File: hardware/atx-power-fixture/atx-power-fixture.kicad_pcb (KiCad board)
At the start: 4 copper layers, 111.8 x 64.4 mm, 33 parts, among them J1 ATX24RH, J2 Screw_Terminal_01x02, J3 BINDING_POST, J4 BINDING_POST, J5 Console FTDI, Q1 DMG2301L, Q2 2N7002, SW1 SW_SPST, SW2 SW_SPST, U1 SSD1306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

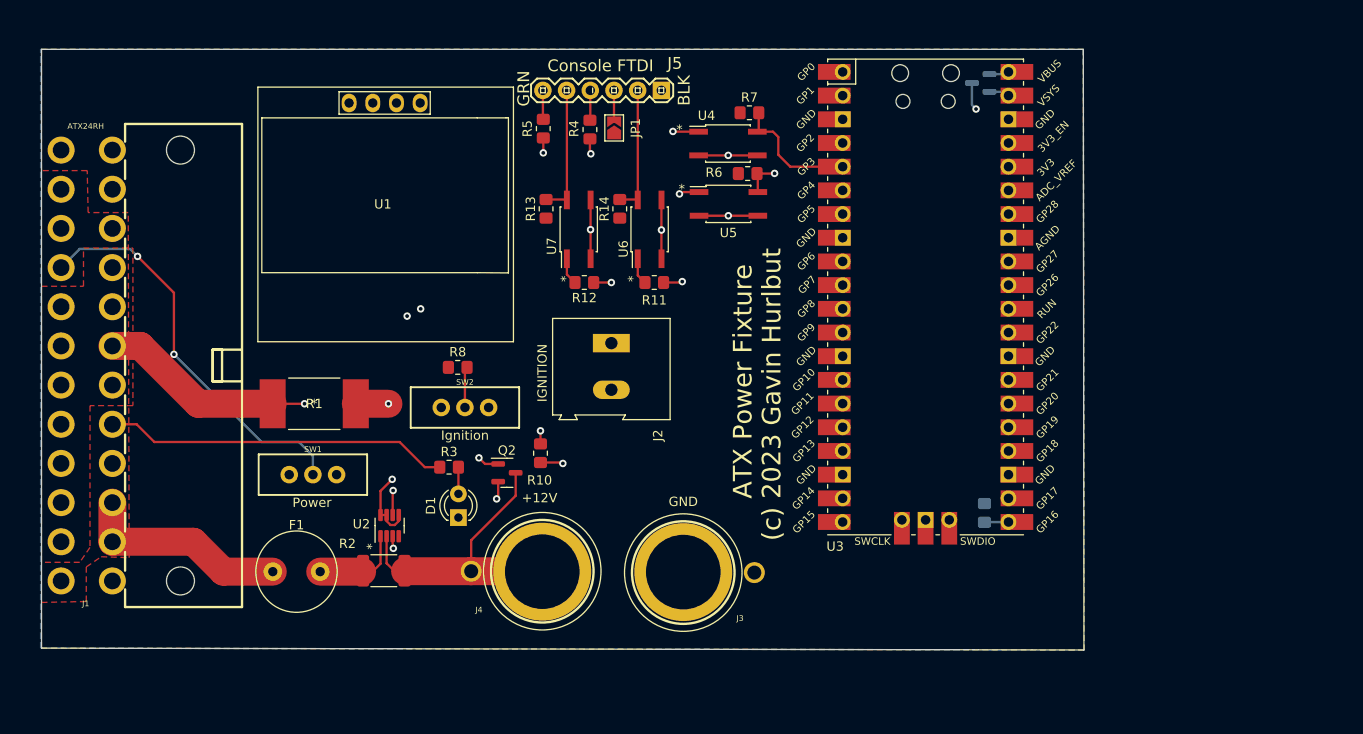
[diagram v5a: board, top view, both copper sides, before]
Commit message: Someone put the ATX connector on back-asswards.  Ooops.
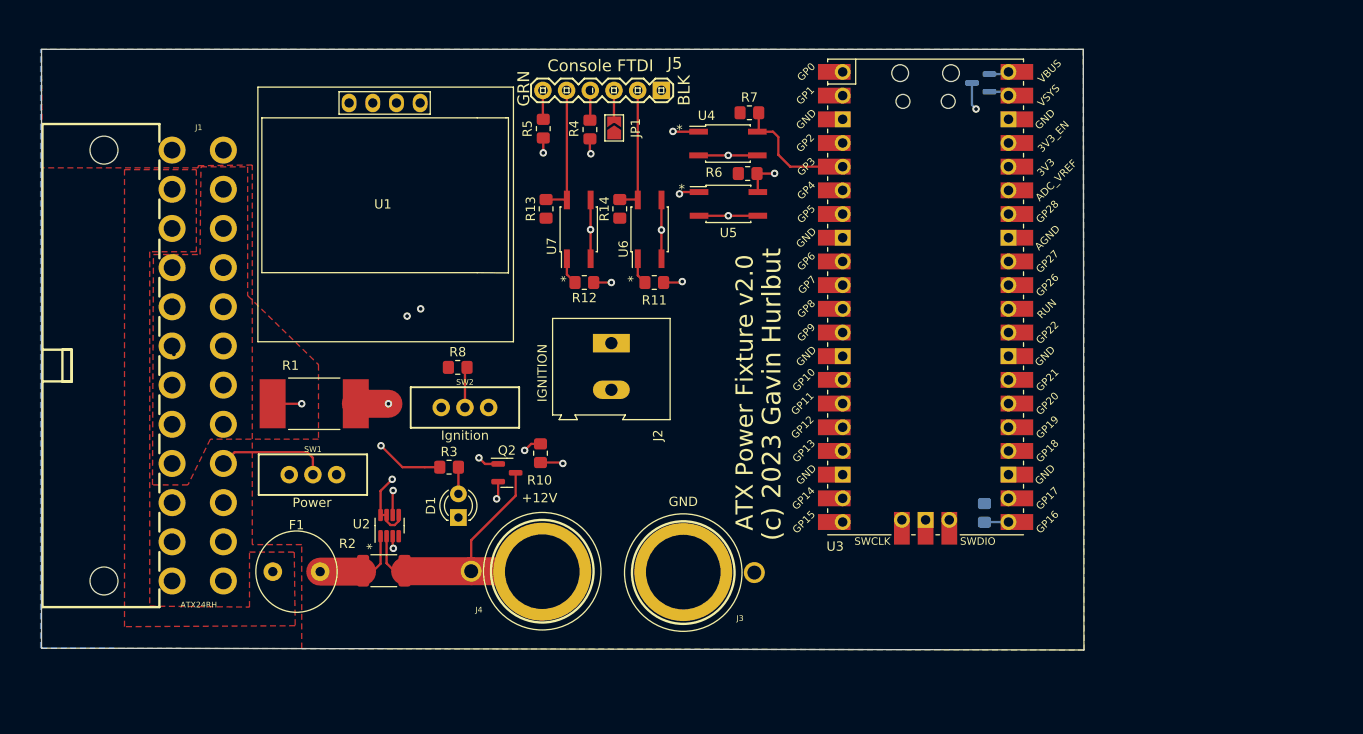
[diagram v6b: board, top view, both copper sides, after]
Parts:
- moved J1 3.12 mm to (98.0, 85.7), turned to -90 degrees
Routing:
- net Net-(J1-Pad16): track 43.1 -> 12.1 mm, vias 2 -> 0
- net +12Vin: track 22.7 -> 0.00 mm
- net +5V: track 116.8 -> 96.9 mm
- net LocalRTS: track 30.0 -> 26.7 mm
- net LocalTX: track 39.7 -> 37.6 mm
- net Net-(R8-Pad2): track 68.7 -> 66.7 mm
- net Net-(J1-Pad8): track 37.0 -> 35.8 mm, vias 0 -> 1
- net GND: track 31.4 -> 32.2 mm, vias 7 -> 8
- added copper zone on F.Cu, net +12Vin
- added copper zone on In1.Cu, net +3V3
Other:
- outline, holes or cut-outs redrawn
- board text added: "ATX Power Fixture v2.0"
- board text removed: "ATX Power Fixture"

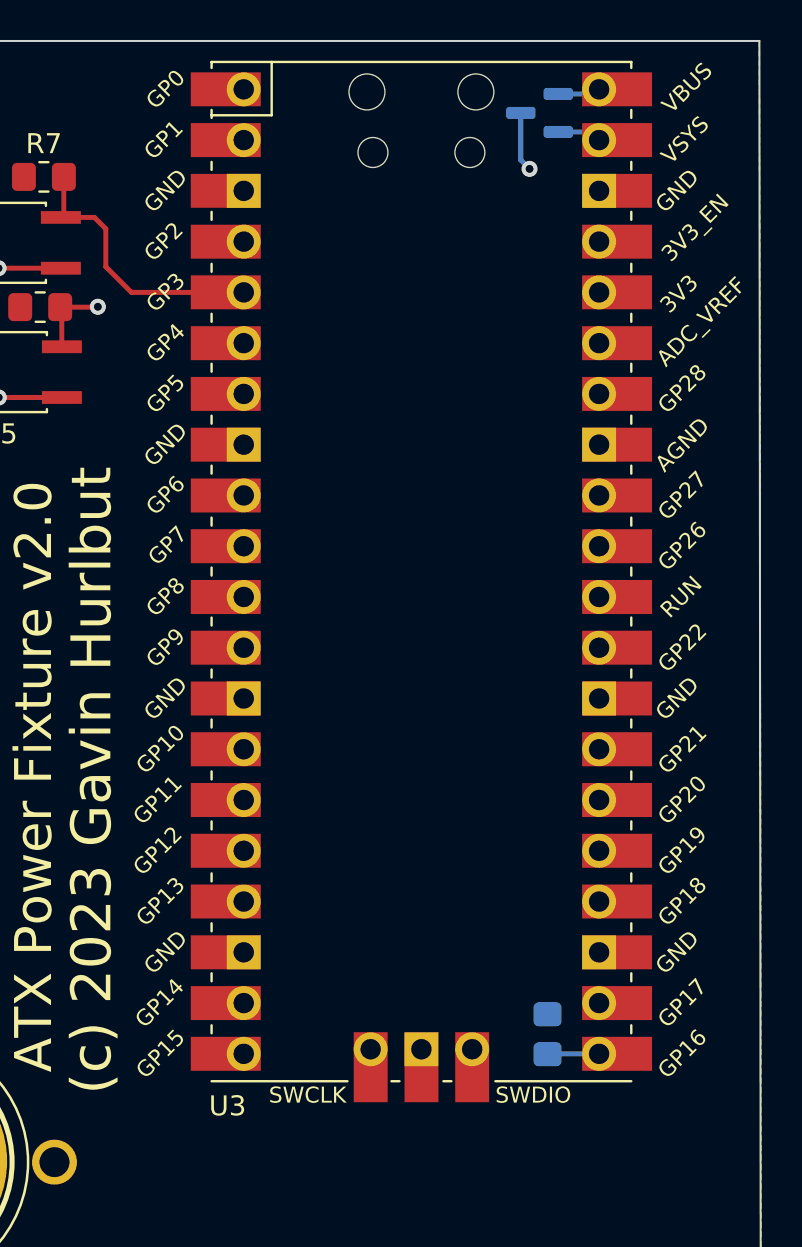
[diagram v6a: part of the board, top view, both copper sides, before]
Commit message: Switch the ATX board to use Pico W
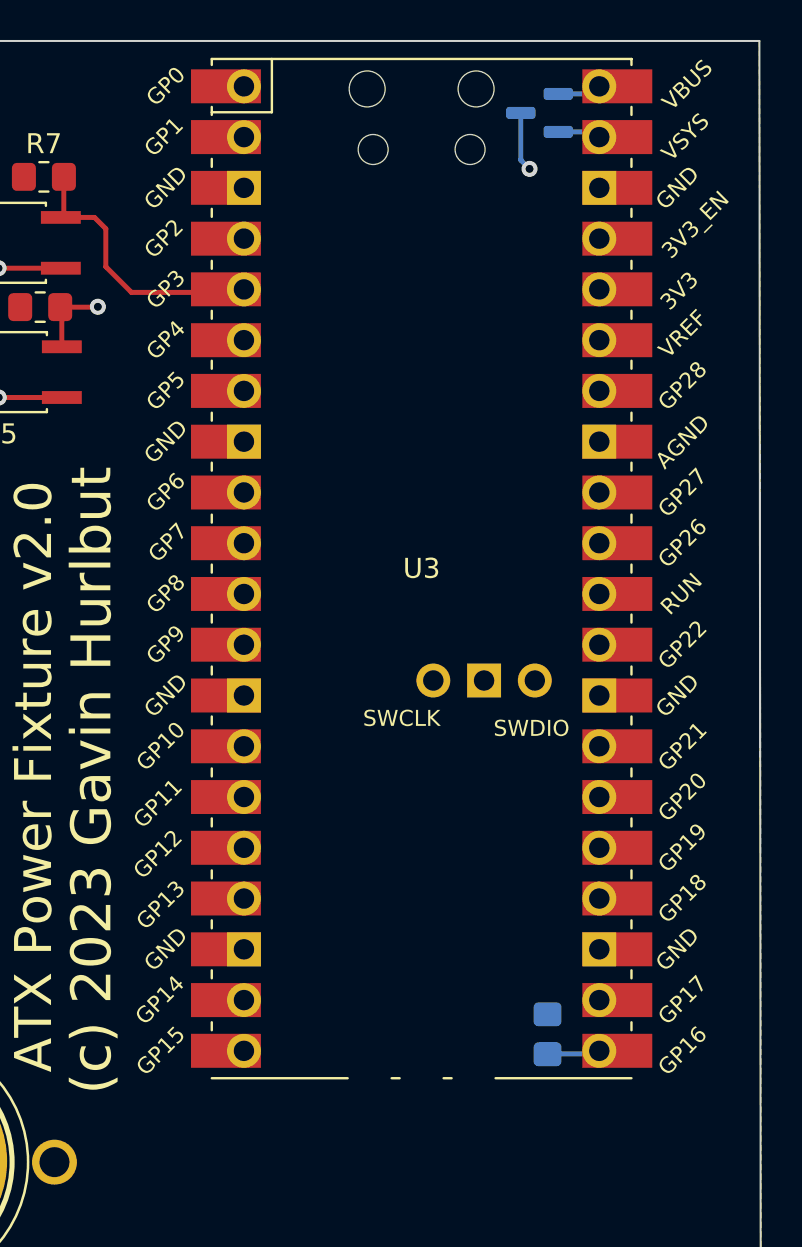
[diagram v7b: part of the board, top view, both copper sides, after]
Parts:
- U3: value Pico -> PicoW; footprint RPi_Pico:RPi_Pico_SMD_TH -> RPi_Pico:RPi_PicoW_SMD_TH
- moved U3 0.15 mm to (183.6, 78.2)

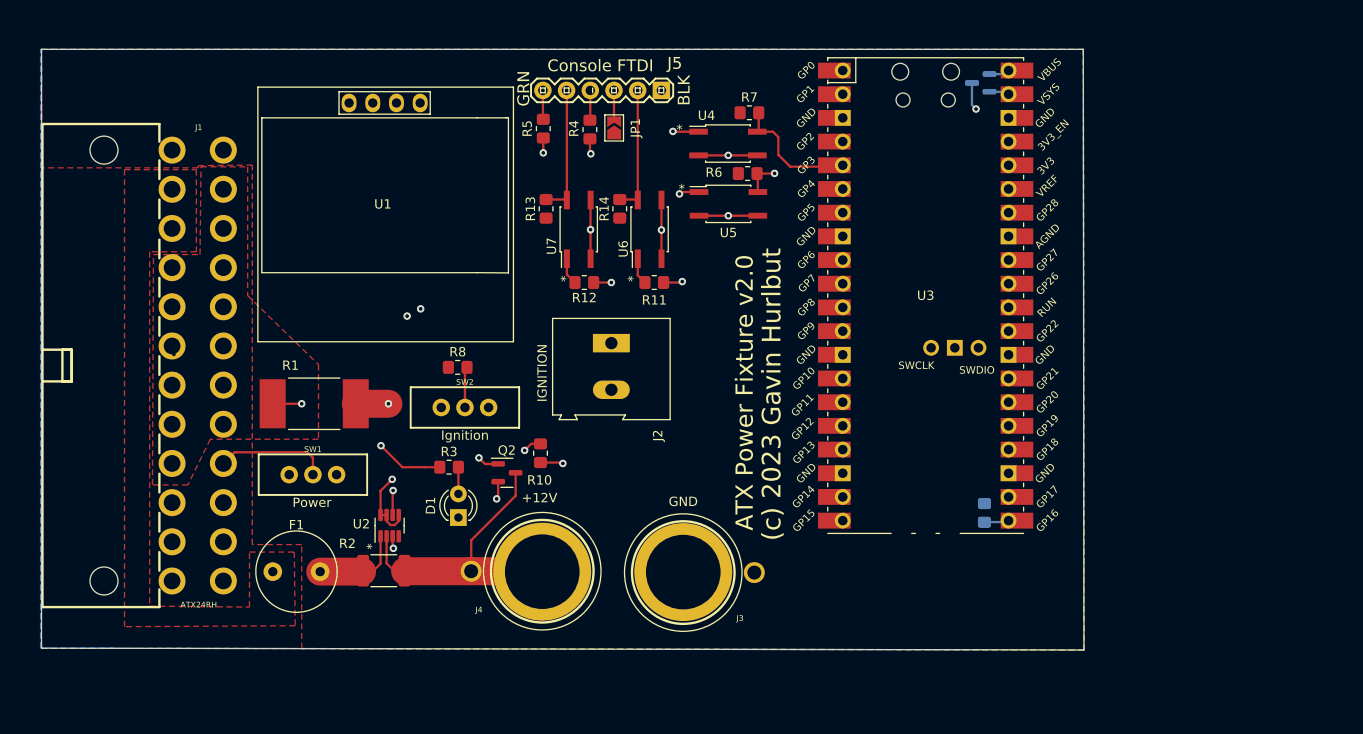
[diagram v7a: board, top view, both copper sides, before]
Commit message: Converted atx-power-fixture to PlatformIO, and to STM32F042F6
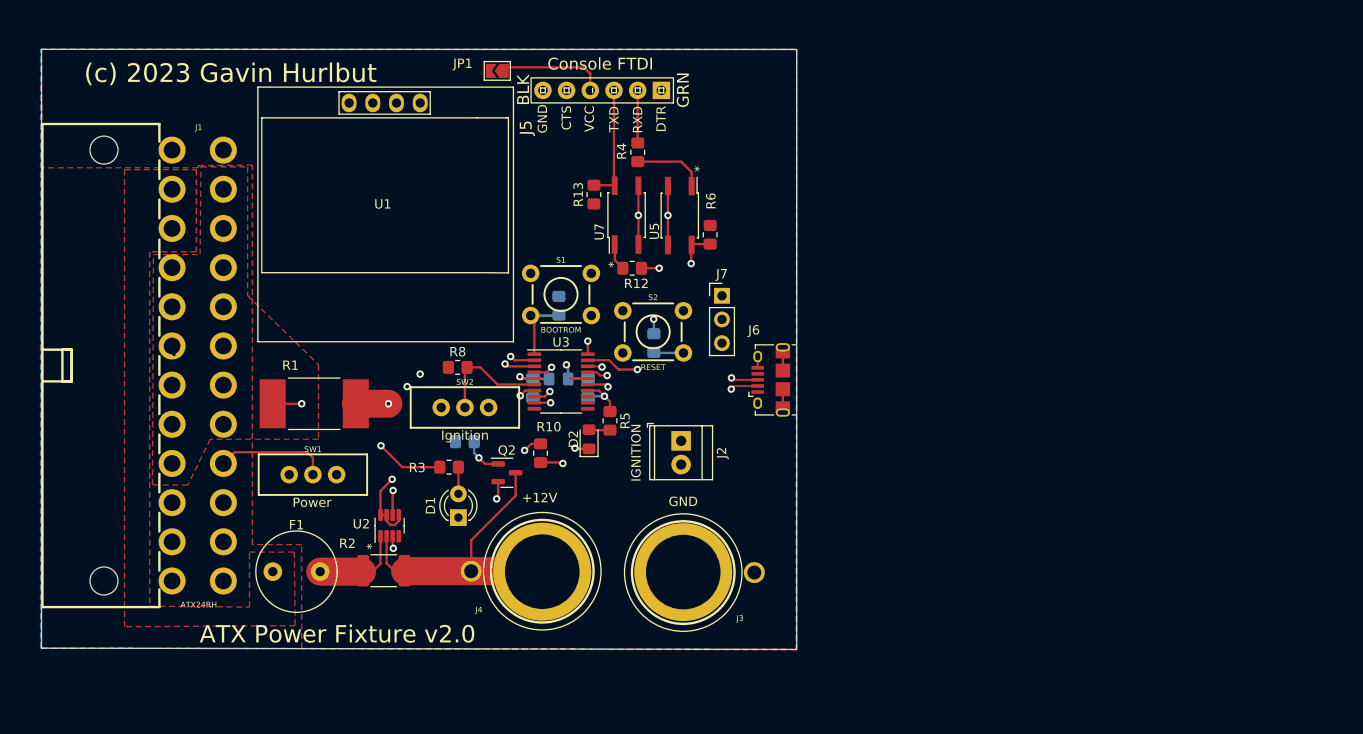
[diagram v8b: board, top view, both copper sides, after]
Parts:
- removed Q1: DMG2301L, Package_TO_SOT_SMD:SOT-23
- removed R14: 10k, Resistor_SMD:R_0805_2012Metric_Pad1.20x1.40mm_HandSolder
- removed U4, U6: LTV-355T, Package_SO:SO-4_4.4x3.6mm_P2.54mm
- added C1: 100nF, Capacitor_SMD:C_0805_2012Metric_Pad1.18x1.45mm_HandSolder, B.Cu at (147.4, 88.1)
- added C2: 100nF, Capacitor_SMD:C_0805_2012Metric_Pad1.18x1.45mm_HandSolder, B.Cu at (141.5, 88.1)
- added D2: LED, LED_SMD:LED_0805_2012Metric_Pad1.15x1.40mm_HandSolder, F.Cu at (147.5, 93.6)
- added FB1: Ferrite, Inductor_SMD:L_0805_2012Metric_Pad1.15x1.40mm_HandSolder, B.Cu at (144.2, 87.1)
- added J6: USB_B_Micro, Connector_USB:USB_Micro-B_Amphenol_10118194_Horizontal, F.Cu at (167.0, 87.2)
- added J7: SWD, Connector_PinHeader_2.54mm:PinHeader_1x03_P2.54mm_Vertical, F.Cu at (161.8, 78.2)
- added S1: BOOTROM, SparkFun-Switches:TACTILE_SWITCH_PTH_6.0MM, F.Cu at (144.5, 78.1)
- added S2: RESET, SparkFun-Switches:TACTILE_SWITCH_PTH_6.0MM, F.Cu at (154.4, 82.1)
- J2: footprint TerminalBlock:TerminalBlock_Altech_AK300-2_P5.00mm -> TerminalBlock_TE-Connectivity:TerminalBlock_TE_282834-2_1x02_P2.54mm_Horizontal
- J5: footprint Beirdo:FTDI_BASIC -> Beirdo:FTDI-TARGET
- R11: value 220R -> 10k; moved to B.Cu
- R5: value 220R -> 330
- R7: moved to B.Cu
- U3: value PicoW -> STM32F042F6Px; footprint RPi_Pico:RPi_PicoW_SMD_TH -> Package_SO:TSSOP-20_4.4x6.5mm_P0.65mm
- moved R9 56.2 mm to (134.2, 93.9), turned to 180 degrees
- moved U3 40.2 mm to (144.5, 87.4)
- moved R5 32.1 mm to (149.8, 91.6)
- moved R7 29.1 mm to (144.3, 79.3), turned to 90 degrees
- moved JP1 13.9 mm to (137.7, 54.1), turned to 180 degrees
- moved J2 12.9 mm to (157.4, 93.8)
- moved R6 7.70 mm to (160.5, 71.7), turned to -90 degrees
- moved R11 6.49 mm to (154.5, 83.3), turned to -90 degrees
- moved R4 5.68 mm to (152.7, 62.8)
- moved U5 5.36 mm to (157.2, 69.6), turned to -90 degrees
- moved R12 5.35 mm to (152.1, 75.3)
- moved R13 5.35 mm to (148.0, 67.4)
- moved U7 5.35 mm to (151.5, 69.6)
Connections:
- J5 pad 1: GND -> unconnected-(J5-Pad1)
- J5 pad 2: ConsoleCTS -> ConsoleRX
- J5 pad 3: Net-(J5-Pad3) -> ConsoleTX
- J5 pad 4: ConsoleTX -> Net-(J5-Pad4)
- J5 pad 5: ConsoleRX -> unconnected-(J5-Pad5)
- J5 pad 6: ConsoleRTS -> GND
- JP1 pad 1: +3V3 -> Net-(J5-Pad4)
- JP1 pad 2: Net-(J5-Pad3) -> +3V3
- Q2 pad 1: Net-(Q2-Pad1) -> IGNITION_EN
- R11 pad 1: LocalRTS -> +3V3
- R11 pad 2: Net-(R11-Pad2) -> ~{RESET}
- R13 pad 2: ConsoleRX -> ConsoleTX
- R4 pad 1: ConsoleTX -> ConsoleRX
- R5 pad 1: ConsoleRTS -> Net-(R5-Pad1)
- R7 pad 1: +3V3 -> Net-(R7-Pad1)
- R7 pad 2: LocalCTS -> GND
- R8 pad 2: Net-(R8-Pad2) -> ~{IGNITION_SW}
- R9 pad 1: Net-(Q2-Pad1) -> IGNITION_EN
- SW2 pad 2: Net-(R8-Pad2) -> ~{IGNITION_SW}
- U3 pad 1: LocalTX -> Net-(R7-Pad1)
- U3 pad 11: SDA -> unconnected-(U3-Pad11)
- U3 pad 12: SCL -> unconnected-(U3-Pad12)
- U3 pad 13: GND -> unconnected-(U3-Pad13)
- U3 pad 14: unconnected-(U3-Pad14) -> Net-(R5-Pad1)
- U3 pad 15: unconnected-(U3-Pad15) -> GND
- U3 pad 16: unconnected-(U3-Pad16) -> +3V3
- U3 pad 17: unconnected-(U3-Pad17) -> USB_D-
- U3 pad 18: GND -> USB_D+
- U3 pad 19: unconnected-(U3-Pad19) -> SWDIO
- U3 pad 2: LocalRX -> SDA
- U3 pad 20: unconnected-(U3-Pad20) -> SWDCLK
- U3 pad 3: GND -> SCL
- U3 pad 4: LocalRTS -> ~{RESET}
- U3 pad 5: LocalCTS -> /VDDA
- U3 pad 6: unconnected-(U3-Pad6) -> ~{IGNITION_SW}
- U3 pad 7: unconnected-(U3-Pad7) -> IGNITION_EN
- U3 pad 8: GND -> LocalTX
- U3 pad 9: unconnected-(U3-Pad9) -> LocalRX
- U7 pad 4: ConsoleRX -> ConsoleTX
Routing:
- net +5V: track 96.9 -> 3.22 mm, vias 2 -> 1
- net Net-(R8-Pad2): track 66.7 -> 0.00 mm
- net Net-(Q2-Pad1): track 64.5 -> 0.00 mm, vias 1 -> 0
- net SCL: track 96.9 -> 64.2 mm, vias 2 -> 3
- net SDA: track 90.7 -> 58.6 mm, vias 2 -> 3
- net LocalRTS: track 26.7 -> 0.00 mm, vias 1 -> 0
- net ~{RESET}: track 0.00 -> 20.0 mm, vias 0 -> 1
- net USB_D-: track 0.00 -> 19.1 mm, vias 0 -> 2
- net USB_D+: track 0.00 -> 18.8 mm, vias 0 -> 2
- net SWDIO: track 0.00 -> 18.1 mm, vias 0 -> 1
- net Net-(D2-Pad2): track 19.2 -> 2.26 mm, vias 2 -> 0
- net SWDCLK: track 0.00 -> 16.4 mm, vias 0 -> 1
- net LocalTX: track 37.6 -> 22.9 mm, vias 1 -> 2
- net IGNITION_EN: track 0.00 -> 14.5 mm, vias 0 -> 2
- net LocalCTS: track 13.9 -> 0.00 mm
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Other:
- board size 111.8 x 64.4 mm -> 81 x 64.3 mm
